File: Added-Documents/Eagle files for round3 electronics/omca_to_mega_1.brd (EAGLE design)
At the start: 80 x 80 mm, 43 parts, among them IC1 ATMEGA2560-16AU, IC3 ATMEGA644-20PU, J1 22-05-7028-02, J2 22-05-7028-02, J3 22-05-7028-02, J4 22-05-7028-02, Q1 STP5NA50, Q2 STP5NA50, Q3 STP5NA50, Q4 STP5NA50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

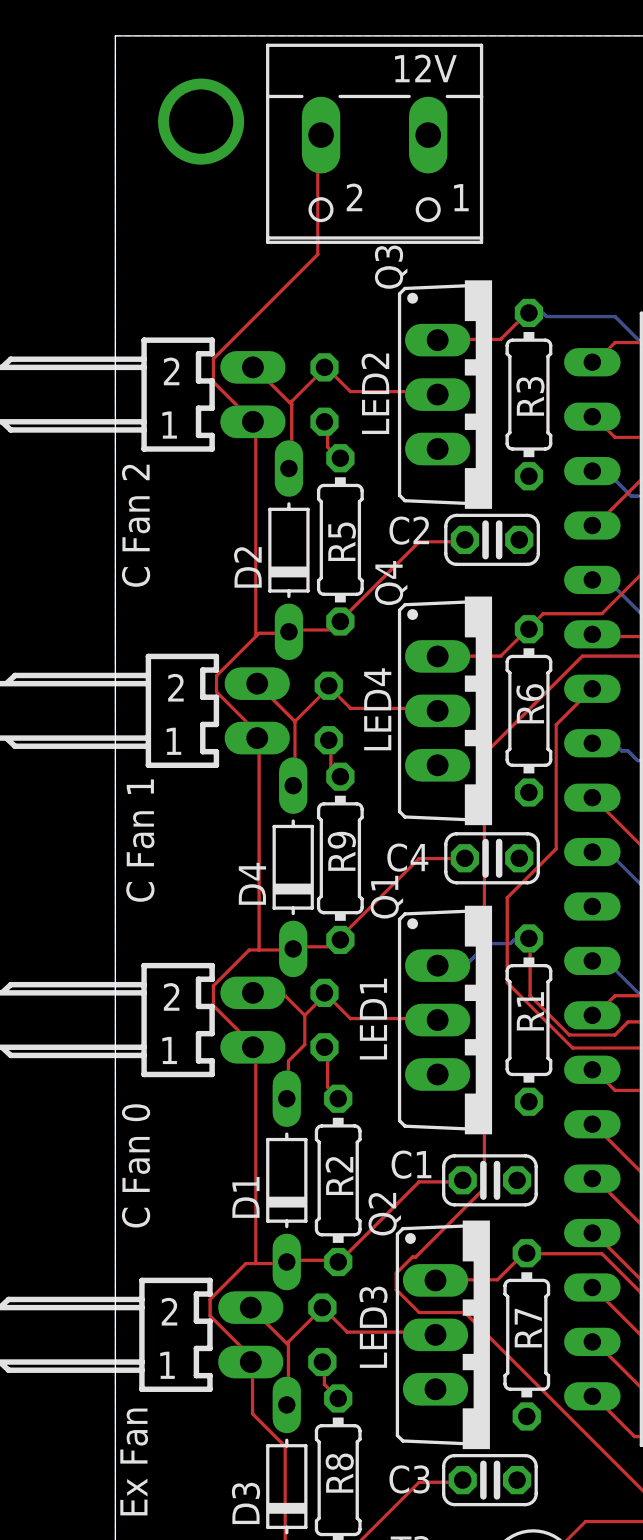
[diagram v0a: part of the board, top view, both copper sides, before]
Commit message: fatter tracks at fet's
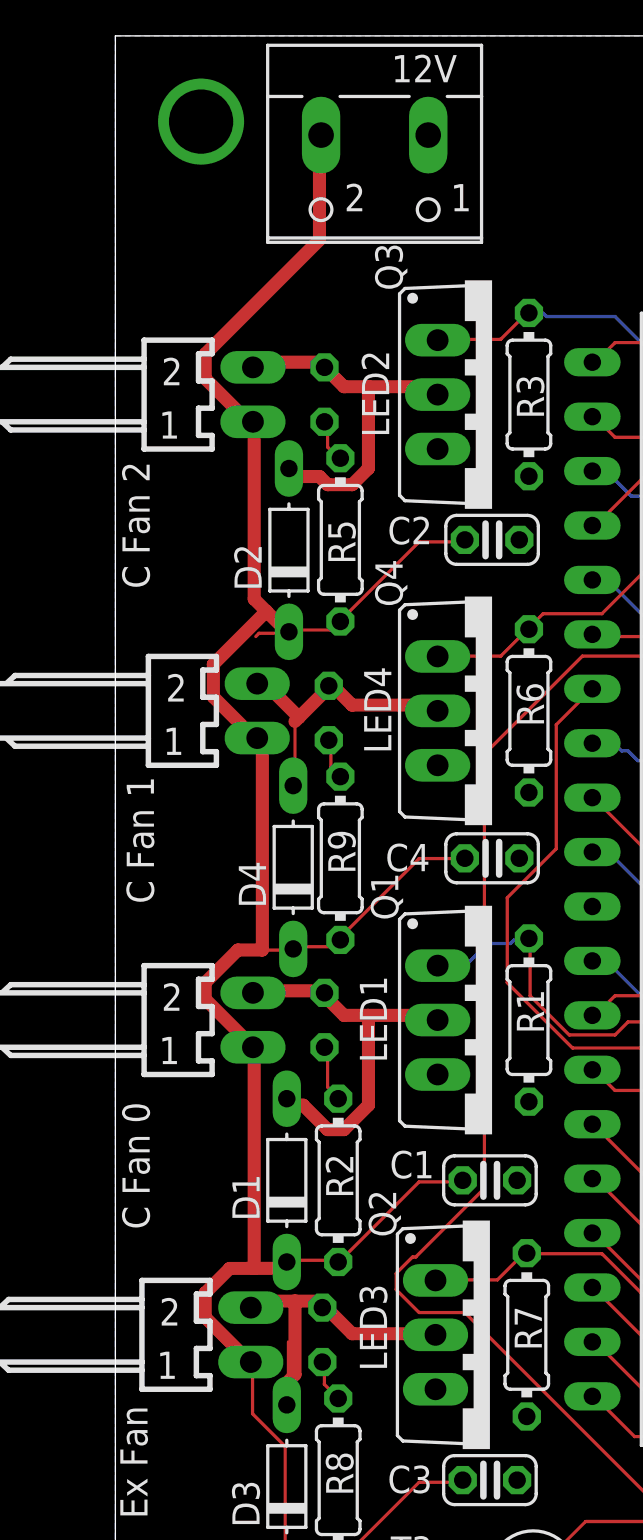
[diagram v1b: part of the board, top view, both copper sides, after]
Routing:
- net 12V: track 120.5 -> 126.4 mm
- net N$2: track 14.3 -> 18.6 mm
- net N$5: track 13.7 -> 17.8 mm
- net N$13: track 13.6 -> 17.5 mm
